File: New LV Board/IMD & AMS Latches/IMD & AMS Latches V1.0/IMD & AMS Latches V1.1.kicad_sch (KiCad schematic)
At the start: 23 parts, among them J2 B12B-PH-K-S, K1 A161CS12VDC.64, K2 A161CS12VDC.64, K3 A161CS12VDC.64, K4 A161CS12VDC.64, K5 A161CS12VDC.64, K6 A161CS12VDC.64, P1 Conn_01x20_MountingPin, P2 Conn_01x20_MountingPin, SW1 Test Reset IMD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

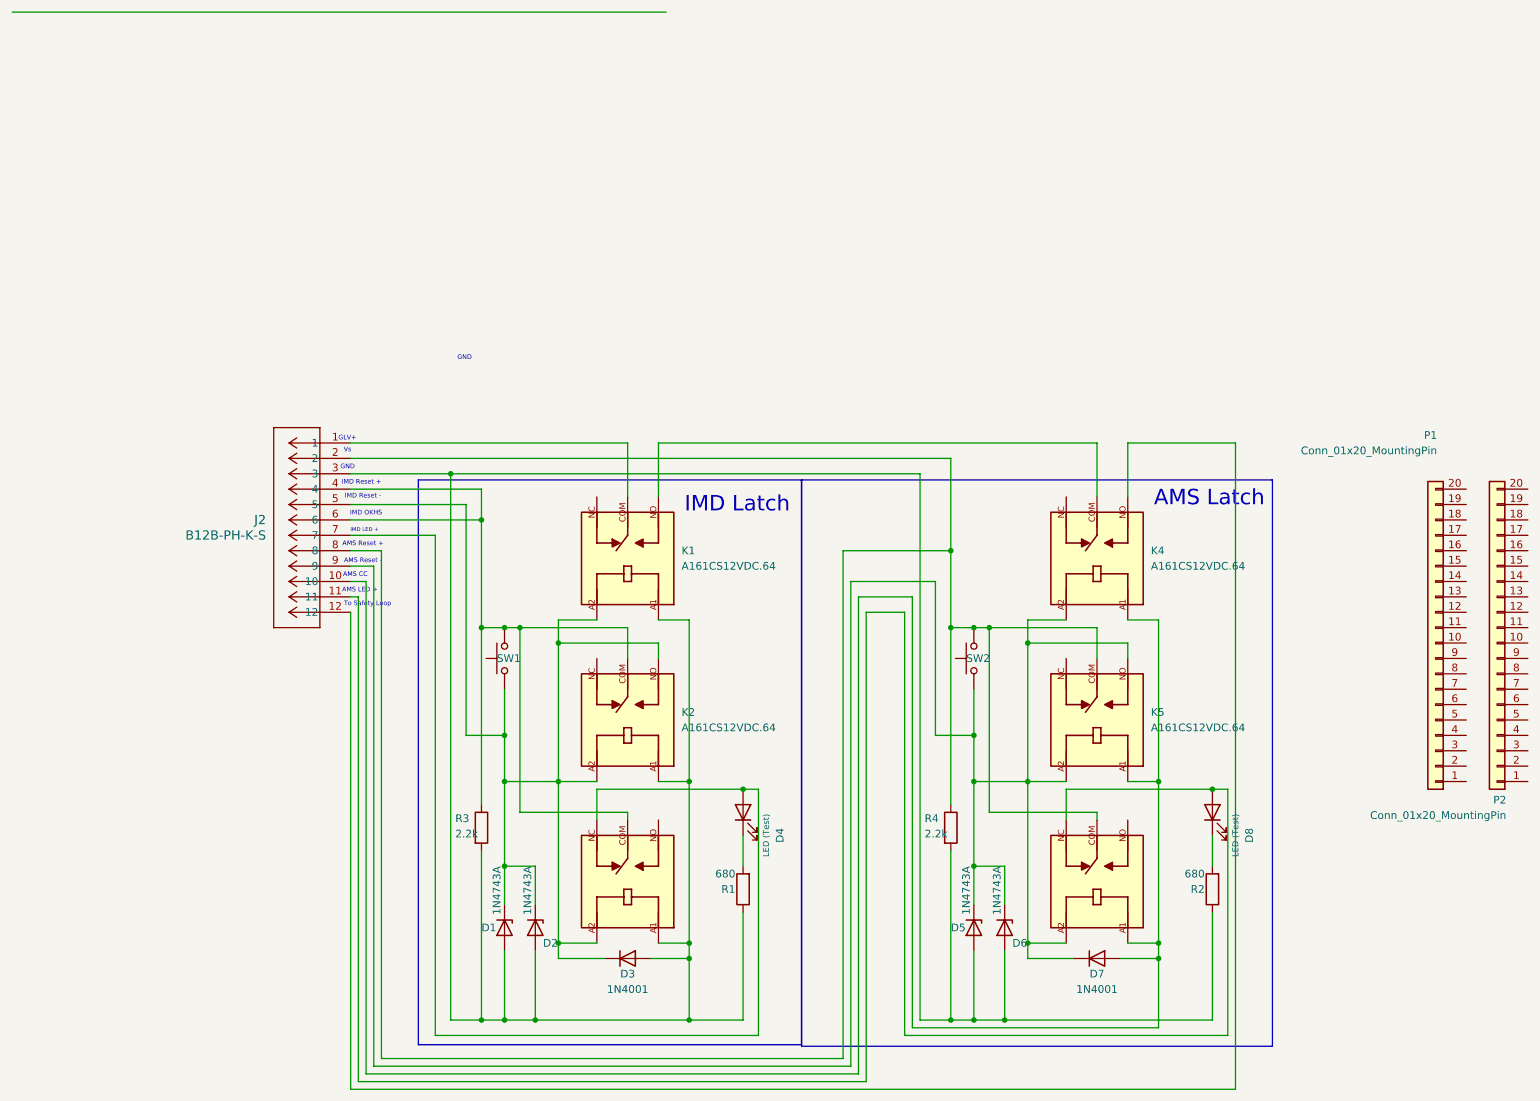
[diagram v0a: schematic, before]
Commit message: AMS & IMD fixing some connections
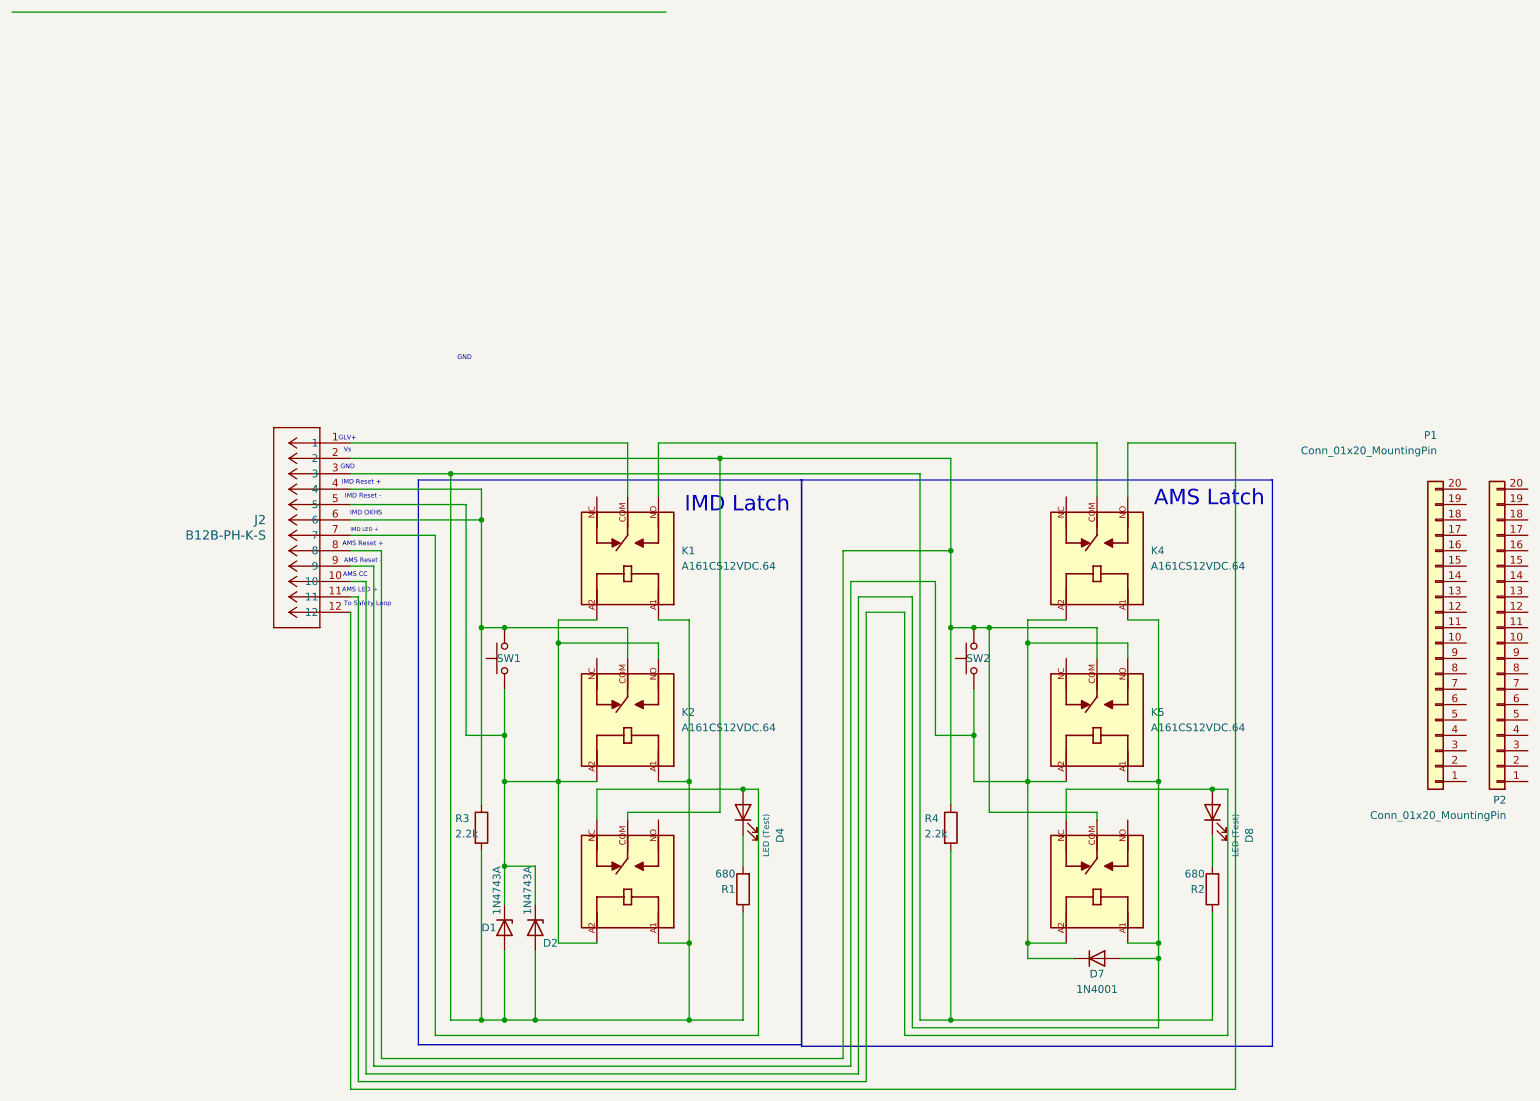
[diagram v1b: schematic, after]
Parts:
- removed D3: 1N4001, Diode_THT:D_DO-41_SOD81_P10.16mm_Horizontal, symbol Diode:1N4001
- removed D5, D6: 1N4743A, motorsports:D_DO-41_SOD81_P3.81mm_Vertical_AnodeUp, symbol Device:D_Zener
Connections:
- net at J2.4, J2.6, K2.COM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: no longer K3.COM
- net at J2.2, J2.8, K5.COM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: now also K3.COM
